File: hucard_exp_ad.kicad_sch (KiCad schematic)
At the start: 27 parts, among them CN102 PCE-EXPANSION-CONN, CN103 PCE_SGX_Hucard_Conn

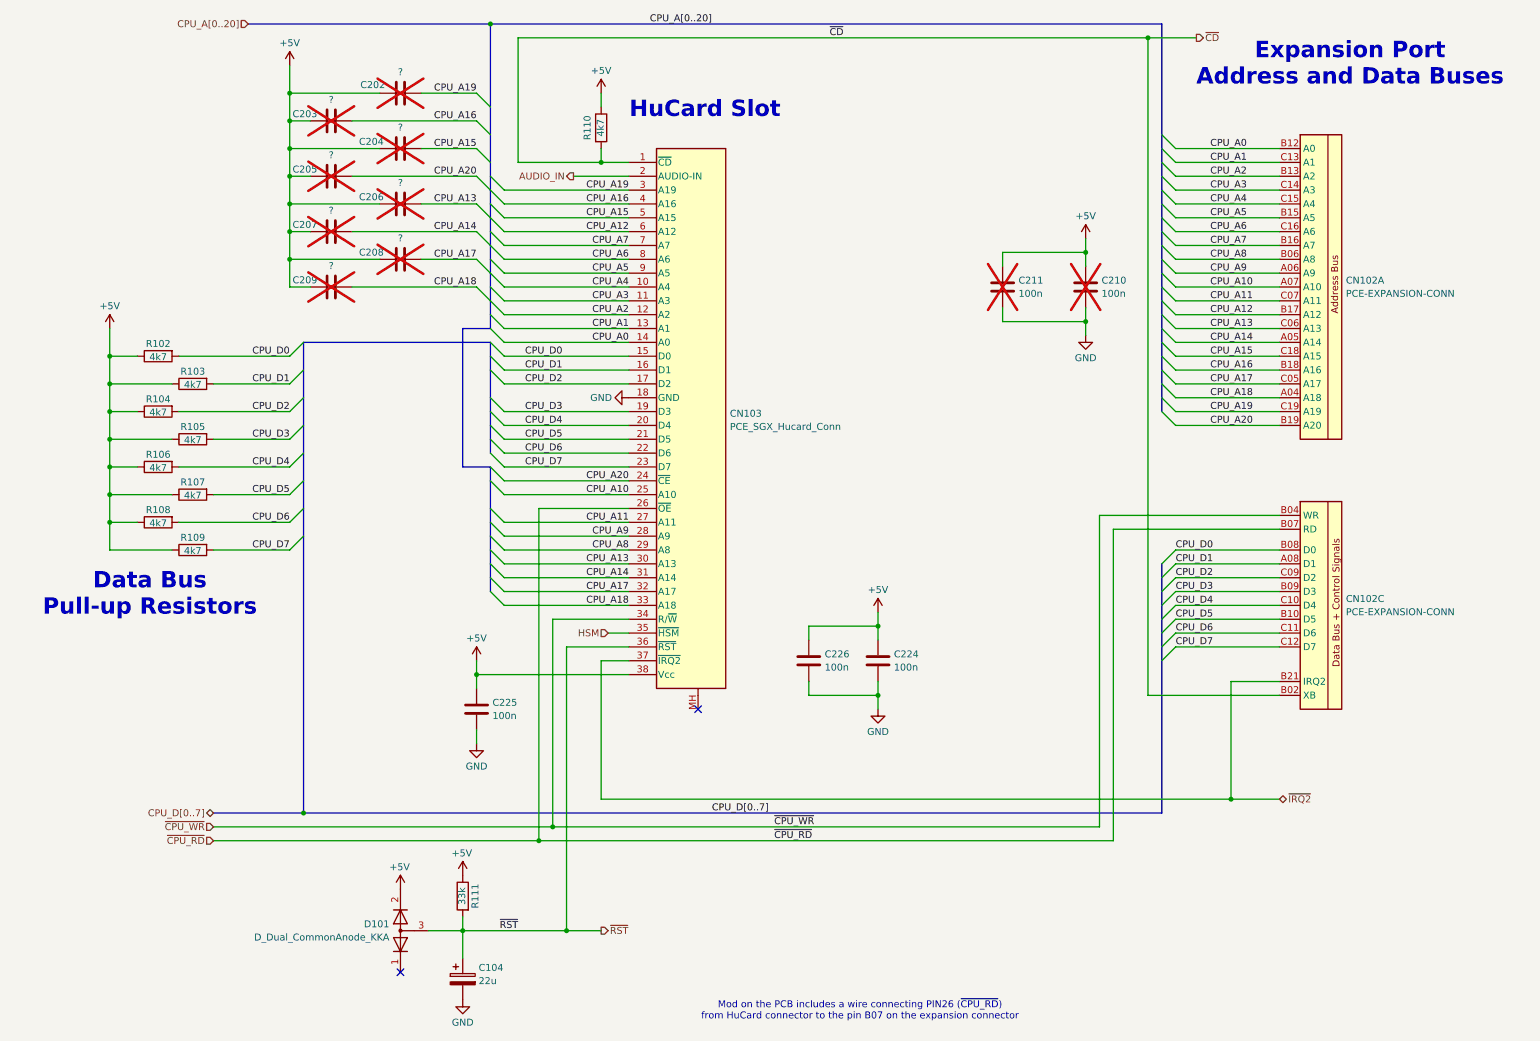
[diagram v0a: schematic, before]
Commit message: Missed out CD dection signal to main CPU and found values of decoupling capacitors under CPU hidden by EMI shield.
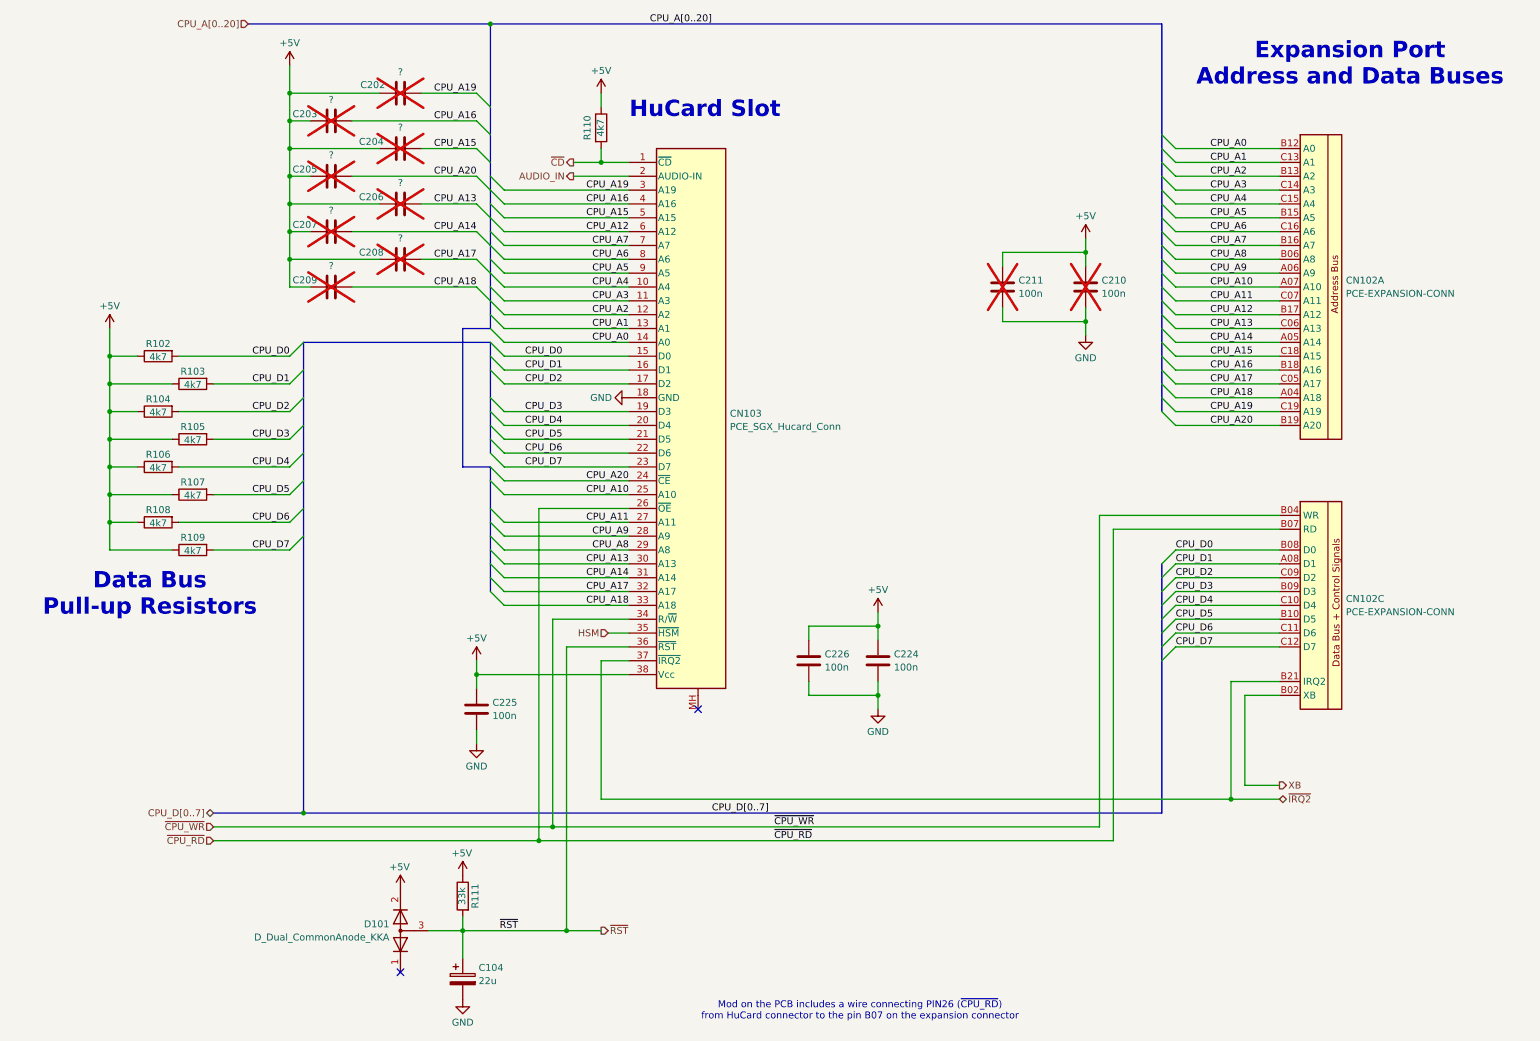
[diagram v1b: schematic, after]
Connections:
- net ~{CD}: no longer CN102.B02 (XB)
- new net XB: CN102.B02 (XB)
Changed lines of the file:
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@@
 	)
 	(junction
-		(at 288.29 43.18)
-		(diameter 0)
-		(color 0 0 0 0)
-	)
-	(junction
 		(at 167.64 40.64)
 		(diameter 0)
@@
 	(wire
 		(pts
+			(xy 312.42 163.83) (xy 306.07 163.83)
+		)
+		(stroke
+			(width 0)
+			(type default)
+		)
+	)
+	(wire
+		(pts
 			(xy 303.53 161.29) (xy 312.42 161.29)
 		)
@@
 		)
 	)
+	(wire
+		(pts
+			(xy 306.07 163.83) (xy 306.07 180.34)
+		)
+		(stroke
+			(width 0)
+			(type default)
+		)
+	)
 	(bus
 		(pts
@@
 	(wire
 		(pts
-			(xy 288.29 43.18) (xy 297.18 43.18)
+			(xy 238.76 161.29) (xy 238.76 163.83)
 		)
 		(stroke
@@
 	(wire
 		(pts
-			(xy 238.76 161.29) (xy 238.76 163.83)
+			(xy 110.49 132.08) (xy 130.81 132.08)
 		)
 		(stroke
@@
 	(wire
 		(pts
-			(xy 110.49 132.08) (xy 130.81 132.08)
+			(xy 306.07 180.34) (xy 312.42 180.34)
 		)
 		(stroke
@@
 	(wire
 		(pts
-			(xy 172.72 43.18) (xy 288.29 43.18)
-		)
-		(stroke
-			(width 0)
-			(type default)
-		)
-	)
-	(wire
-		(pts
 			(xy 187.96 53.34) (xy 187.96 55.88)
 		)
@@
 	(wire
 		(pts
-			(xy 288.29 163.83) (xy 312.42 163.83)
-		)
-		(stroke
-			(width 0)
-			(type default)
-		)
-	)
-	(wire
-		(pts
 			(xy 187.96 66.04) (xy 187.96 63.5)
 		)
@@
 		)
 	)
-	(wire
-		(pts
-			(xy 172.72 66.04) (xy 172.72 43.18)
-		)
-		(stroke
-			(width 0)
-			(type default)
-		)
-	)
 	(bus
 		(pts
@@
 	(wire
 		(pts
-			(xy 172.72 66.04) (xy 187.96 66.04)
+			(xy 182.88 66.04) (xy 187.96 66.04)
 		)
 		(stroke
@@
 		)
 	)
-	(wire
-		(pts
-			(xy 288.29 43.18) (xy 288.29 163.83)
-		)
-		(stroke
-			(width 0)
-			(type default)
-		)
-	)
 	(bus
 		(pts
@@
 		)
 	)
-	(label "~{CD}"
-		(at 229.87 43.18 0)
-		(fields_autoplaced yes)
-		(effects
-			(font
-				(size 1.27 1.27)
-			)
-			(justify left bottom)
-		)
-	)
 	(label "CPU_A14"
 		(at 193.04 142.24 180)
@@
 		)
 	)
+	(hierarchical_label "XB"
+		(shape output)
+		(at 312.42 180.34 0)
+		(fields_autoplaced yes)
+		(effects
+			(font
+				(size 1.27 1.27)
+			)
+			(justify left)
+		)
+	)
 	(hierarchical_label "AUDIO_IN"
 		(shape output)
@@
 	(hierarchical_label "~{CD}"
 		(shape output)
-		(at 297.18 43.18 0)
+		(at 182.88 66.04 180)
 		(fields_autoplaced yes)
 		(effects
@@
 				(size 1.27 1.27)
 			)
-			(justify left)
+			(justify right)
 		)
 	)
